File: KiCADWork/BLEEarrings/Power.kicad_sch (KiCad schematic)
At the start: 14 parts, among them Q1 DMP3013SFV, SW1 PB22E06071, U1 XB6096I2SV, U2 MCP73831T-2ACI/OT

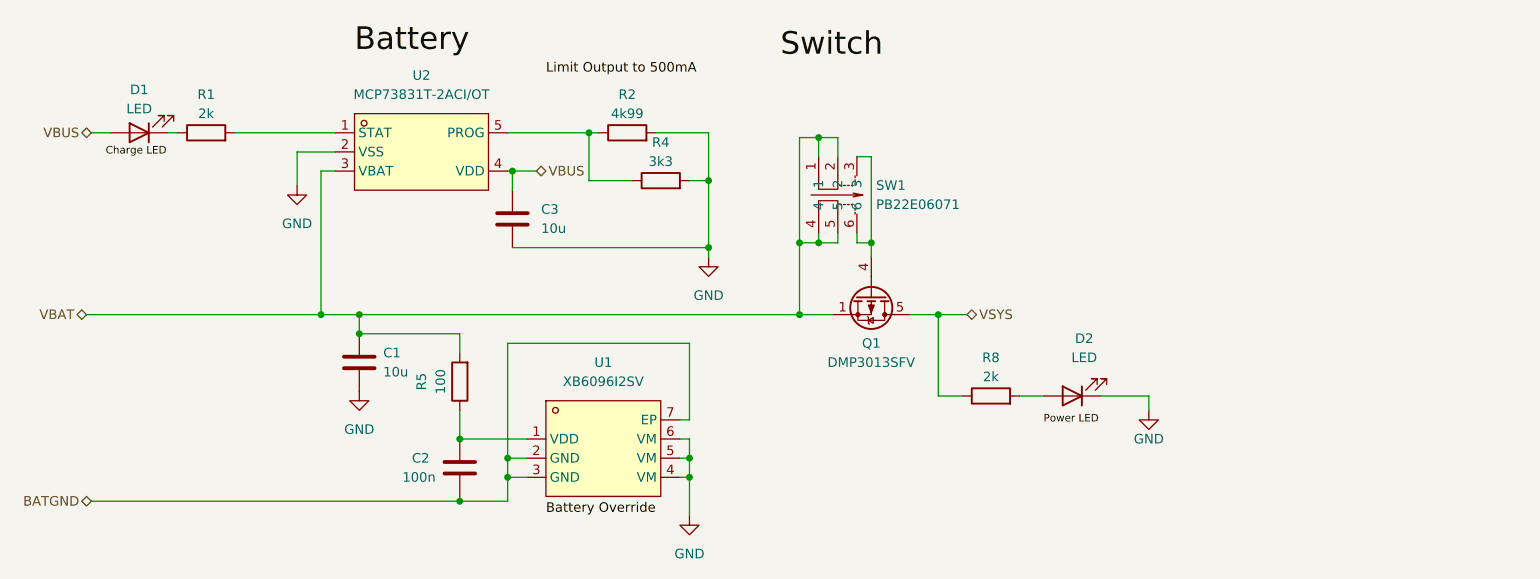
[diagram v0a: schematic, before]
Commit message: First Draft Schematic Done
- Symbols and footprints checked
- Dom added to repo
- Centralised footprints created
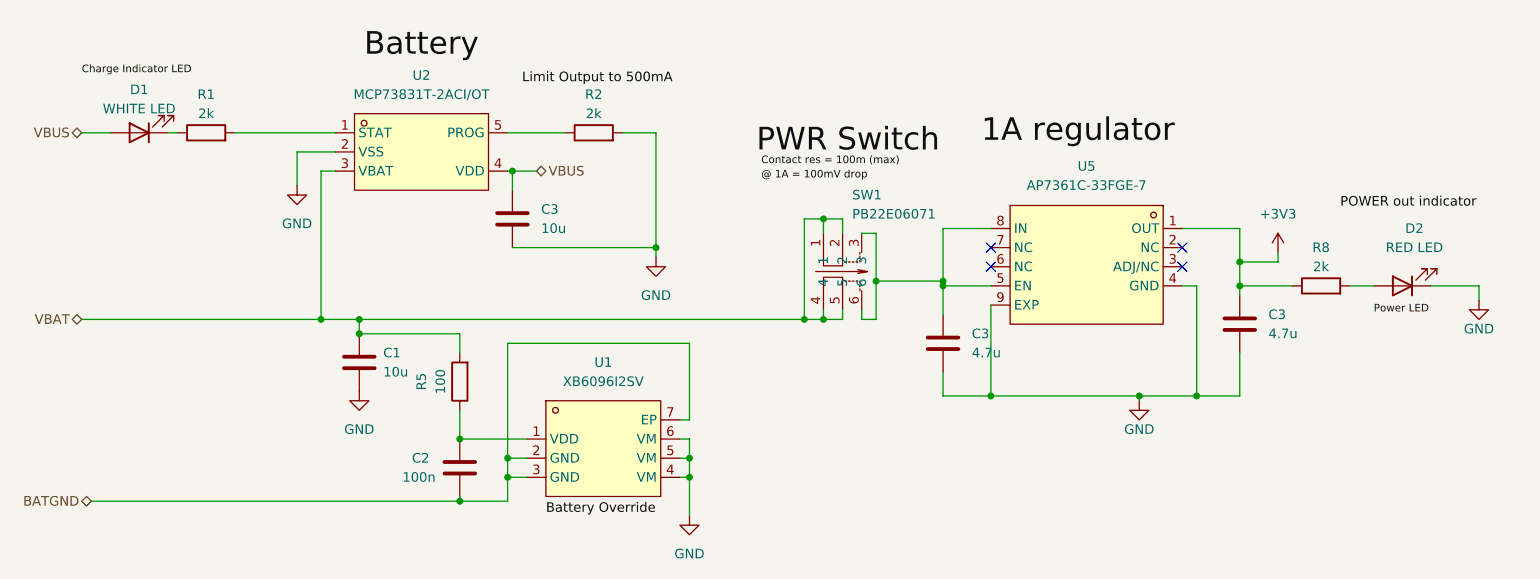
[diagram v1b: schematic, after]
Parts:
- removed Q1: DMP3013SFV, Package_SON:Diodes_PowerDI3333-8, symbol Transistor_FET:DMP3013SFV
- removed R4: 3k3, Resistor_SMD:R_0402_1005Metric, symbol Device:R
- added C3 (x2): 4.7u, Capacitor_SMD:C_0402_1005Metric_Pad0.74x0.62mm_HandSolder, symbol Device:C
- added U5: AP7361C-33FGE-7, easyeda2kicad:DFN-8_L3.0-W3.0-P0.65-BL-EP, symbol easyeda2kicad:AP7361C-33FGE-7
- D1: value LED -> WHITE LED
- D2: value LED -> RED LED
- R1, R5, R8: footprint Resistor_SMD:R_0402_1005Metric -> Resistor_SMD:R_0402_1005Metric_Pad0.72x0.64mm_HandSolder
- R2: value 4k99 -> 2k; footprint Resistor_SMD:R_0402_1005Metric -> Resistor_SMD:R_0402_1005Metric_Pad0.72x0.64mm_HandSolder
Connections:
- net GND: now also C3.2, C3.2, U5.4 (GND), U5.9 (EXP)
- net at SW1.3, SW1.6: now also C3.1, U5.5 (EN), U5.8 (IN)
- net VSYS renamed +3V3
- net +3V3: now also C3.1, U5.1 (OUT)
- no-connect marks 0 -> 4
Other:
- company: (none) -> Kitty and Dom
- title: (none) -> BLEEarrings (Blade Runner)
- moved on the sheet: D2, R2, R8, SW1

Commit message: Improved Antenna Layout
- Initial layout complete
- TO DO:
    - Test points
    - Curved Tracks
    - Silkscreen
    - Check antenna
    - create casing in blender
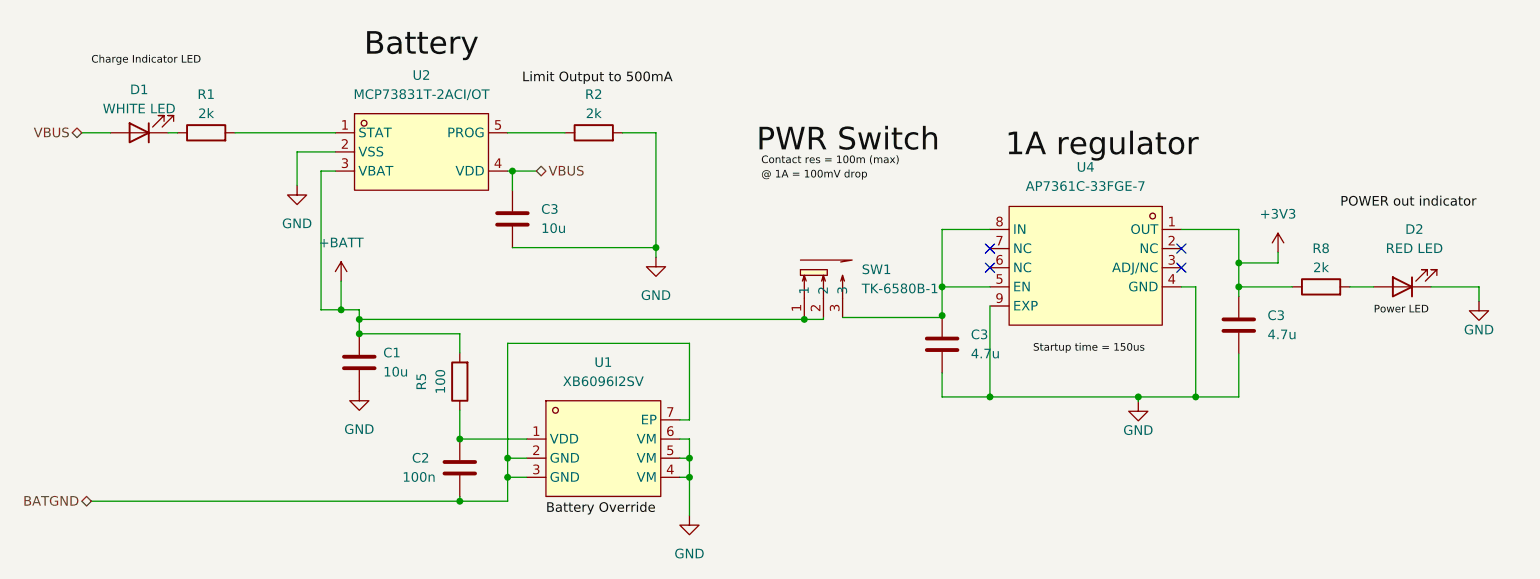
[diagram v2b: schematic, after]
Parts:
- removed SW1: PB22E06071, easyeda2kicad:SW-TH_6P-L5.8-W5.8-P2.00-LS4.5_PB22E06371-0625, symbol easyeda2kicad:PB22E06071
- added SW1: TK-6580B-1, easyeda2kicad:SW-TH_TK-6580B-1, symbol easyeda2kicad:TK-6580B-1
- renumbered U5 to U4
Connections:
- net at C3.1, U4.5 (EN), U4.8 (IN): now also SW1.3
- net VBAT renamed +BATT
- net +BATT: now also SW1.1, SW1.2
